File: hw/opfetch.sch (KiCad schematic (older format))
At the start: 11 parts

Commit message: annotated more components
Also some more work on connecting modules together
and adding glue logic.
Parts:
- gave numbers to parts that had none: 5
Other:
- note added: "opcode fetch logic"
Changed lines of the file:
@@
 -DIS
 $Comp
-L 74LS00 U?
+L 74LS00 U401
 U 1 1 59284C1B
 P 2650 1000
-F 0 "U?" H 2650 1050 50  0000 C CNN
+F 0 "U401" H 2650 1050 50  0000 C CNN
 F 1 "74LS00" H 2650 900 50  0000 C CNN
 F 2 "" H 2650 1000 50  0001 C CNN
@@
 $EndComp
 $Comp
-L 74LS00 U?
+L 74LS00 U401
 U 2 1 59284C82
 P 2650 1600
-F 0 "U?" H 2650 1650 50  0000 C CNN
+F 0 "U401" H 2650 1650 50  0000 C CNN
 F 1 "74LS00" H 2650 1500 50  0000 C CNN
 F 2 "" H 2650 1600 50  0001 C CNN
@@
 $EndComp
 $Comp
-L 74LS193 U?
+L 74LS193 U402
 U 1 1 59284D07
 P 5450 1900
-F 0 "U?" H 5450 2050 50  0000 C CNN
+F 0 "U402" H 5450 2050 50  0000 C CNN
 F 1 "74LS193" H 5450 1900 50  0000 C CNN
 F 2 "" H 5450 1900 50  0001 C CNN
@@
 $EndComp
 $Comp
-L 74LS175 U?
+L 74LS175 U404
 U 1 1 59284D99
 P 5400 4200
-F 0 "U?" H 5400 4200 50  0000 C CNN
+F 0 "U404" H 5400 4200 50  0000 C CNN
 F 1 "74LS175" H 5500 3800 50  0000 C CNN
 F 2 "" H 5400 4200 50  0001 C CNN
@@
 $EndComp
 $Comp
-L 74LS02 U?
+L 74LS02 U403
 U 1 1 59285C63
 P 8100 1600
-F 0 "U?" H 8100 1650 50  0000 C CNN
+F 0 "U403" H 8100 1650 50  0000 C CNN
 F 1 "74LS02" H 8150 1550 50  0000 C CNN
 F 2 "" H 8100 1600 50  0001 C CNN
@@
 $EndComp
 $Comp
-L 74LS02 U?
+L 74LS02 U403
 U 2 1 59285CBA
 P 9600 1600
-F 0 "U?" H 9600 1650 50  0000 C CNN
+F 0 "U403" H 9600 1650 50  0000 C CNN
 F 1 "74LS02" H 9650 1550 50  0000 C CNN
 F 2 "" H 9600 1600 50  0001 C CNN
@@
 $EndComp
 $Comp
-L 74LS02 U?
+L 74LS02 U403
 U 3 1 59285CDB
 P 8100 2500
-F 0 "U?" H 8100 2550 50  0000 C CNN
+F 0 "U403" H 8100 2550 50  0000 C CNN
 F 1 "74LS02" H 8150 2450 50  0000 C CNN
 F 2 "" H 8100 2500 50  0001 C CNN
@@
 $EndComp
 $Comp
-L 74LS02 U?
+L 74LS02 U403
 U 4 1 59285CFE
 P 9600 2150
-F 0 "U?" H 9600 2200 50  0000 C CNN
+F 0 "U403" H 9600 2200 50  0000 C CNN
 F 1 "74LS02" H 9650 2100 50  0000 C CNN
 F 2 "" H 9600 2150 50  0001 C CNN
@@
 wrOpReg
 $Comp
-L 74LS00 U?
+L 74LS00 U401
 U 3 1 59286333
 P 3150 5900
-F 0 "U?" H 3150 5950 50  0000 C CNN
+F 0 "U401" H 3150 5950 50  0000 C CNN
 F 1 "74LS00" H 3150 5800 50  0000 C CNN
 F 2 "" H 3150 5900 50  0001 C CNN
@@
 $EndComp
 $Comp
-L 74LS00 U?
+L 74LS00 U401
 U 4 1 5928636E
 P 3150 6400
-F 0 "U?" H 3150 6450 50  0000 C CNN
+F 0 "U401" H 3150 6450 50  0000 C CNN
 F 1 "74LS00" H 3150 6300 50  0000 C CNN
 F 2 "" H 3150 6400 50  0001 C CNN
@@
 opfetchEnd
 $Comp
-L 74LS574 U?
+L 74LS574 U405
 U 1 1 59287645
 P 8700 5250
-F 0 "U?" H 8700 5250 50  0000 C CNN
+F 0 "U405" H 8700 5250 50  0000 C CNN
 F 1 "74LS574" H 8750 4900 50  0000 C CNN
 F 2 "" H 8700 5250 50  0001 C CNN
@@
 Text Notes 8350 4600 0    60   ~ 0
 opcode register
+Text Notes 7150 6750 0    60   ~ 0
+opcode fetch logic
 $EndSCHEMATC

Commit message: added ucode output registers
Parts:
- U401: value 74LS00 -> 74HC00
- U402: value 74LS193 -> 74HC193
- U403: value 74LS02 -> 74HC02
- U404: value 74LS175 -> 74HC175
- U405: value 74LS574 -> 74HC574
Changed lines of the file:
@@
 P 2650 1000
 F 0 "U401" H 2650 1050 50  0000 C CNN
-F 1 "74LS00" H 2650 900 50  0000 C CNN
+F 1 "74HC00" H 2650 900 50  0000 C CNN
 F 2 "" H 2650 1000 50  0001 C CNN
 F 3 "" H 2650 1000 50  0001 C CNN
@@
 P 2650 1600
 F 0 "U401" H 2650 1650 50  0000 C CNN
-F 1 "74LS00" H 2650 1500 50  0000 C CNN
+F 1 "74HC00" H 2650 1500 50  0000 C CNN
 F 2 "" H 2650 1600 50  0001 C CNN
 F 3 "" H 2650 1600 50  0001 C CNN
@@
 P 5450 1900
 F 0 "U402" H 5450 2050 50  0000 C CNN
-F 1 "74LS193" H 5450 1900 50  0000 C CNN
+F 1 "74HC193" H 5450 1900 50  0000 C CNN
 F 2 "" H 5450 1900 50  0001 C CNN
 F 3 "" H 5450 1900 50  0001 C CNN
@@
 P 5400 4200
 F 0 "U404" H 5400 4200 50  0000 C CNN
-F 1 "74LS175" H 5500 3800 50  0000 C CNN
+F 1 "74HC175" H 5500 3800 50  0000 C CNN
 F 2 "" H 5400 4200 50  0001 C CNN
 F 3 "" H 5400 4200 50  0001 C CNN
@@
 P 8100 1600
 F 0 "U403" H 8100 1650 50  0000 C CNN
-F 1 "74LS02" H 8150 1550 50  0000 C CNN
+F 1 "74HC02" H 8150 1550 50  0000 C CNN
 F 2 "" H 8100 1600 50  0001 C CNN
 F 3 "" H 8100 1600 50  0001 C CNN
@@
 P 9600 1600
 F 0 "U403" H 9600 1650 50  0000 C CNN
-F 1 "74LS02" H 9650 1550 50  0000 C CNN
+F 1 "74HC02" H 9650 1550 50  0000 C CNN
 F 2 "" H 9600 1600 50  0001 C CNN
 F 3 "" H 9600 1600 50  0001 C CNN
@@
 P 8100 2500
 F 0 "U403" H 8100 2550 50  0000 C CNN
-F 1 "74LS02" H 8150 2450 50  0000 C CNN
+F 1 "74HC02" H 8150 2450 50  0000 C CNN
 F 2 "" H 8100 2500 50  0001 C CNN
 F 3 "" H 8100 2500 50  0001 C CNN
@@
 P 9600 2150
 F 0 "U403" H 9600 2200 50  0000 C CNN
-F 1 "74LS02" H 9650 2100 50  0000 C CNN
+F 1 "74HC02" H 9650 2100 50  0000 C CNN
 F 2 "" H 9600 2150 50  0001 C CNN
 F 3 "" H 9600 2150 50  0001 C CNN
@@
 P 3150 5900
 F 0 "U401" H 3150 5950 50  0000 C CNN
-F 1 "74LS00" H 3150 5800 50  0000 C CNN
+F 1 "74HC00" H 3150 5800 50  0000 C CNN
 F 2 "" H 3150 5900 50  0001 C CNN
 F 3 "" H 3150 5900 50  0001 C CNN
@@
 P 3150 6400
 F 0 "U401" H 3150 6450 50  0000 C CNN
-F 1 "74LS00" H 3150 6300 50  0000 C CNN
+F 1 "74HC00" H 3150 6300 50  0000 C CNN
 F 2 "" H 3150 6400 50  0001 C CNN
 F 3 "" H 3150 6400 50  0001 C CNN
@@
 P 8700 5250
 F 0 "U405" H 8700 5250 50  0000 C CNN
-F 1 "74LS574" H 8750 4900 50  0000 C CNN
+F 1 "74HC574" H 8750 4900 50  0000 C CNN
 F 2 "" H 8700 5250 50  0001 C CNN
 F 3 "" H 8700 5250 50  0001 C CNN

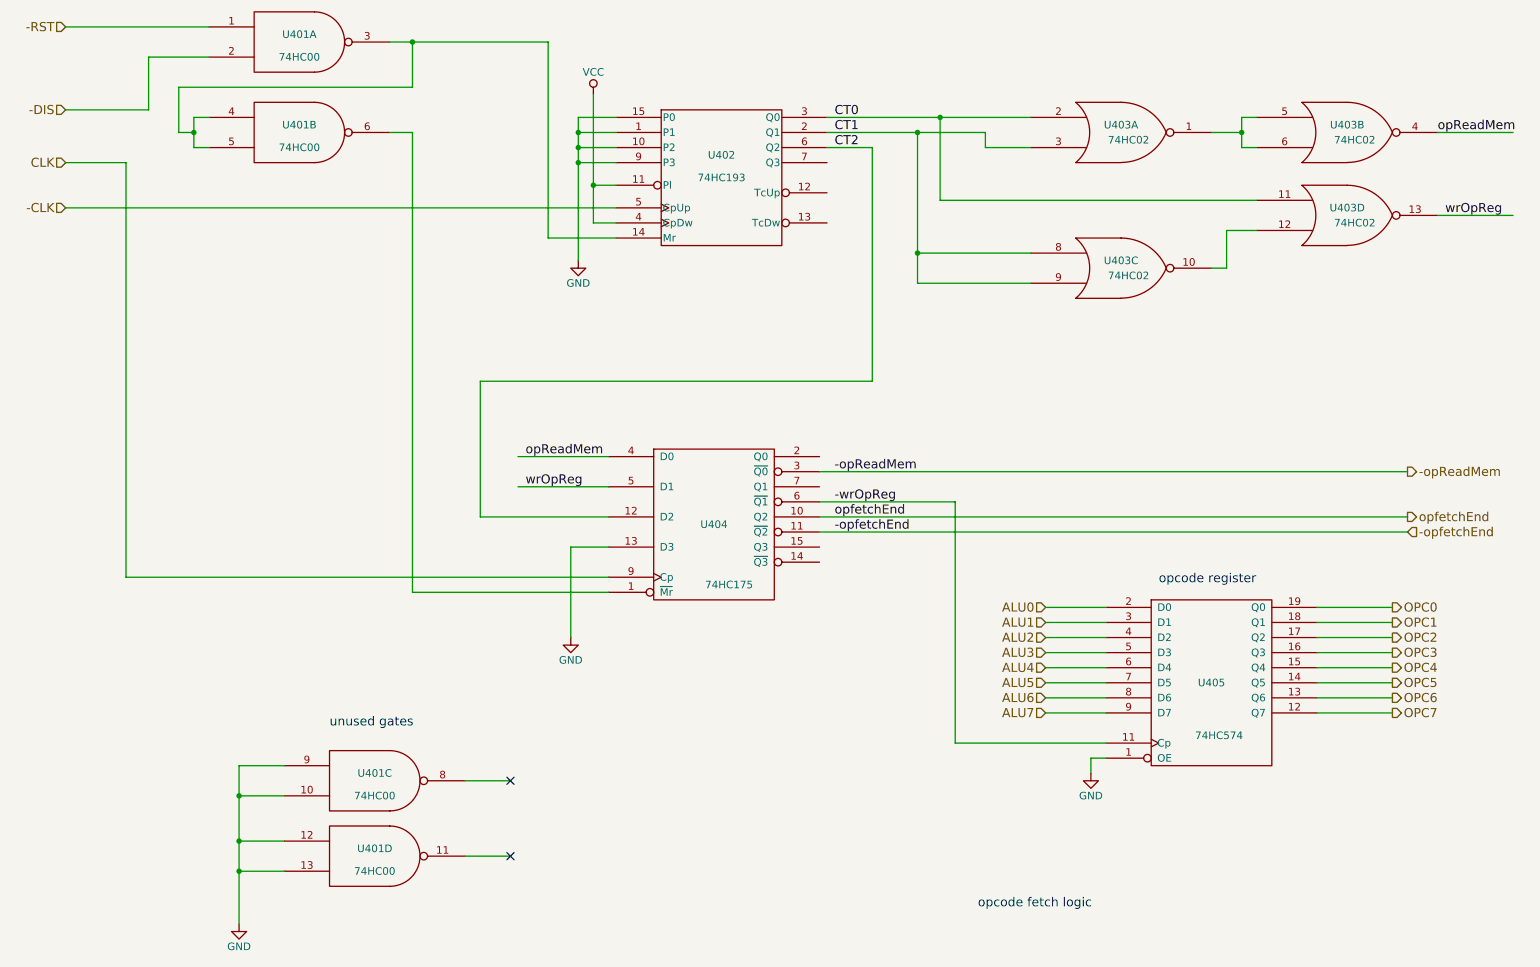
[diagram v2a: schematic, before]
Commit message: tweak opfetch logic to increment PC
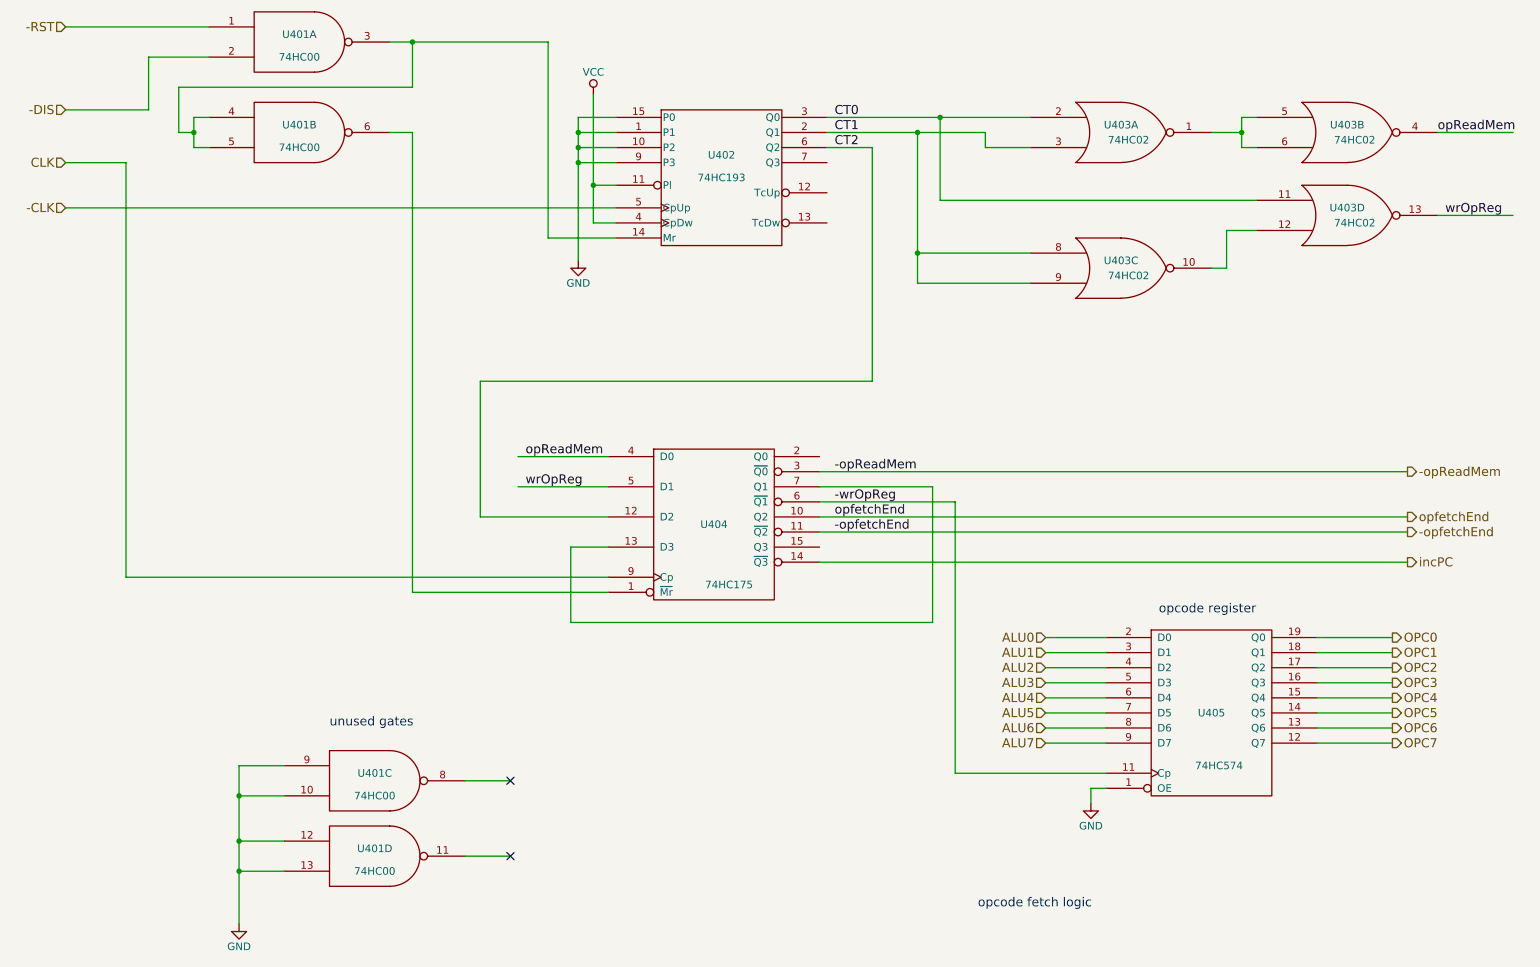
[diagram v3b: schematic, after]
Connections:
- net labels added: incPC
- wire segments 87 -> 91
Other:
- moved on the sheet: U405
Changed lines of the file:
@@
 	1    0    0    -1
 $EndComp
-Text HLabel 7600 4750 0    60   Input ~ 0
+Text HLabel 7600 4950 0    60   Input ~ 0
 ALU0
-Text HLabel 7600 4850 0    60   Input ~ 0
+Text HLabel 7600 5050 0    60   Input ~ 0
 ALU1
-Text HLabel 7600 4950 0    60   Input ~ 0
+Text HLabel 7600 5150 0    60   Input ~ 0
 ALU2
-Text HLabel 7600 5050 0    60   Input ~ 0
+Text HLabel 7600 5250 0    60   Input ~ 0
 ALU3
-Text HLabel 7600 5150 0    60   Input ~ 0
+Text HLabel 7600 5350 0    60   Input ~ 0
 ALU4
-Text HLabel 7600 5250 0    60   Input ~ 0
+Text HLabel 7600 5450 0    60   Input ~ 0
 ALU5
-Text HLabel 7600 5350 0    60   Input ~ 0
+Text HLabel 7600 5550 0    60   Input ~ 0
 ALU6
-Text HLabel 7600 5450 0    60   Input ~ 0
+Text HLabel 7600 5650 0    60   Input ~ 0
 ALU7
 $Comp
@@
 	1500 1800 1100 1800
 Wire Wire Line
-	4750 2200 4600 2200
-Wire Wire Line
-	4600 2200 4600 1350
+	4600 2200 4750 2200
+Wire Wire Line
+	4600 1350 4600 2200
 Wire Wire Line
 	4750 1950 4600 1950
 Connection ~ 4600 1950
 Wire Wire Line
-	4750 1800 4500 1800
+	4500 1800 4750 1800
 Wire Wire Line
 	4500 1500 4500 2450
@@
 	7200 1700 7500 1700
 Wire Wire Line
-	7500 2600 6750 2600
-Wire Wire Line
-	6750 2600 6750 1600
+	6750 2600 7500 2600
+Wire Wire Line
+	6750 1600 6750 2600
 Connection ~ 6750 1600
 Wire Wire Line
@@
 Wire Wire Line
 	4700 4350 4450 4350
-Wire Wire Line
-	4450 4350 4450 4950
-$Comp
-L GND #PWR?
-U 1 1 59286A61
-P 4450 4950
-F 0 "#PWR?" H 4450 4700 50  0001 C CNN
-F 1 "GND" H 4450 4800 50  0000 C CNN
-F 2 "" H 4450 4950 50  0001 C CNN
-F 3 "" H 4450 4950 50  0001 C CNN
-	1    4450 4950
-	1    0    0    -1
-$EndComp
 Text Label 4150 3750 0    60   ~ 0
 opReadMem
@@
 L 74LS574 U405
 U 1 1 59287645
-P 8700 5250
-F 0 "U405" H 8700 5250 50  0000 C CNN
-F 1 "74HC574" H 8750 4900 50  0000 C CNN
-F 2 "" H 8700 5250 50  0001 C CNN
-F 3 "" H 8700 5250 50  0001 C CNN
-	1    8700 5250
-	1    0    0    -1
-$EndComp
-Wire Wire Line
-	8000 5650 7000 5650
-Wire Wire Line
-	7000 5650 7000 4050
-Wire Wire Line
-	8000 5750 7900 5750
-Wire Wire Line
-	7900 5750 7900 5850
+P 8700 5450
+F 0 "U405" H 8700 5450 50  0000 C CNN
+F 1 "74HC574" H 8750 5100 50  0000 C CNN
+F 2 "" H 8700 5450 50  0001 C CNN
+F 3 "" H 8700 5450 50  0001 C CNN
+	1    8700 5450
+	1    0    0    -1
+$EndComp
+Wire Wire Line
+	8000 5850 7000 5850
+Wire Wire Line
+	7000 5850 7000 4050
+Wire Wire Line
+	8000 5950 7900 5950
+Wire Wire Line
+	7900 5950 7900 6050
 $Comp
 L GND #PWR?
 U 1 1 59287754
-P 7900 5850
-F 0 "#PWR?" H 7900 5600 50  0001 C CNN
-F 1 "GND" H 7900 5700 50  0000 C CNN
-F 2 "" H 7900 5850 50  0001 C CNN
-F 3 "" H 7900 5850 50  0001 C CNN
-	1    7900 5850
-	1    0    0    -1
-$EndComp
-Wire Wire Line
-	8000 4750 7600 4750
-Wire Wire Line
-	8000 4850 7600 4850
+P 7900 6050
+F 0 "#PWR?" H 7900 5800 50  0001 C CNN
+F 1 "GND" H 7900 5900 50  0000 C CNN
+F 2 "" H 7900 6050 50  0001 C CNN
+F 3 "" H 7900 6050 50  0001 C CNN
+	1    7900 6050
+	1    0    0    -1
+$EndComp
 Wire Wire Line
 	8000 4950 7600 4950
@@
 Wire Wire Line
 	8000 5450 7600 5450
-Text HLabel 9900 4750 2    60   Output ~ 0
+Wire Wire Line
+	8000 5550 7600 5550
+Wire Wire Line
+	8000 5650 7600 5650
+Text HLabel 9900 4950 2    60   Output ~ 0
 OPC0
-Text HLabel 9900 4850 2    60   Output ~ 0
+Text HLabel 9900 5050 2    60   Output ~ 0
 OPC1
-Text HLabel 9900 4950 2    60   Output ~ 0
+Text HLabel 9900 5150 2    60   Output ~ 0
 OPC2
-Text HLabel 9900 5050 2    60   Output ~ 0
+Text HLabel 9900 5250 2    60   Output ~ 0
 OPC3
-Text HLabel 9900 5150 2    60   Output ~ 0
+Text HLabel 9900 5350 2    60   Output ~ 0
 OPC4
-Text HLabel 9900 5250 2    60   Output ~ 0
+Text HLabel 9900 5450 2    60   Output ~ 0
 OPC5
-Text HLabel 9900 5350 2    60   Output ~ 0
+Text HLabel 9900 5550 2    60   Output ~ 0
 OPC6
-Text HLabel 9900 5450 2    60   Output ~ 0
+Text HLabel 9900 5650 2    60   Output ~ 0
 OPC7
 Wire Wire Line
-	9400 4750 9900 4750
-Wire Wire Line
-	9400 4850 9900 4850
-Wire Wire Line
 	9400 4950 9900 4950
 Wire Wire Line
@@
 Wire Wire Line
 	9400 5450 9900 5450
+Wire Wire Line
+	9400 5550 9900 5550
+Wire Wire Line
+	9400 5650 9900 5650
 Wire Wire Line
 	6150 1700 6450 1700
@@
 Text Notes 2850 5550 0    60   ~ 0
 unused gates
-Text HLabel 10000 4250 2    60   Input ~ 0
+Text HLabel 10000 4250 2    60   Output ~ 0
 -opfetchEnd
 Wire Wire Line
@@
 Text Label 6200 4250 0    60   ~ 0
 -opfetchEnd
-Text Notes 8350 4600 0    60   ~ 0
+Text Notes 8350 4800 0    60   ~ 0
 opcode register
 Text Notes 7150 6750 0    60   ~ 0
 opcode fetch logic
+Wire Wire Line
+	6100 3950 6850 3950
+Wire Wire Line
+	6850 3950 6850 4850
+Wire Wire Line
+	6850 4850 4450 4850
+Wire Wire Line
+	4450 4850 4450 4350
+Wire Wire Line
+	6100 4450 10000 4450
+Text HLabel 10000 4450 2    60   Output ~ 0
+incPC
 $EndSCHEMATC

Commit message: more work on glue logic
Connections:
- net labels added: opIncPC
- net labels removed: incPC
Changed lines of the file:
@@
 	6100 4450 10000 4450
 Text HLabel 10000 4450 2    60   Output ~ 0
-incPC
+opIncPC
 $EndSCHEMATC
